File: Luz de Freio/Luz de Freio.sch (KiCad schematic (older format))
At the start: 40 parts, among them J1 Screw_Terminal_01x02, J2 Screw_Terminal_01x02, K1 RELAY_19.1x15.5mm, Q1 BC548, Q2 IRF3205, U1 MC34063AP, U2 TL431DBZ, U3 LM358

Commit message: atualizacao esquematico
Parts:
- added G?: Logo_e-Power_Large, e-Power:Logo_e-Power_16.5x8.0mm_SilkS, symbol e-Power:Logo_e-Power_Large
- added G?: Logo_UFRGS_Large, e-Power:Logo_UFRGS_14.7x8.0mm_SilkS, symbol e-Power:Logo_UFRGS_Large
- added R19: 1R, Resistor_SMD:R_0805_2012Metric, symbol Device:R
- added R20, R21: 10K, Resistor_SMD:R_0805_2012Metric, symbol Device:R
- added R22, R23: 100K, Resistor_SMD:R_0805_2012Metric, symbol Device:R
- added TP1: 24V, e-Power:TestPoint_Pad_D1.0mm, symbol Connector:TestPoint
- added TP2: GND, e-Power:TestPoint_Pad_D1.0mm, symbol Connector:TestPoint
- added TP3: 1.25V, e-Power:TestPoint_Pad_D1.0mm, symbol Connector:TestPoint
- C1: value 100uF -> 220uF; footprint Capacitor_SMD:C_0805_2012Metric_Pad1.15x1.40mm_HandSolder -> e-Power:CP_Elec_10x10
- C3: value 100uF -> 220uF
- D1: value 1N5819 -> SS54HF
- D3, J1, J2: footprint Connector_Phoenix_GMSTB:PhoenixContact_GMSTBA_2,5_2-G-7,62_1x02_P7.62mm_Horizontal -> e-Power:TerminalBlock_Phoenix_MKDS-1,5-2_1x02_P5.08mm_Horizontal_3D
- L1: value 170uH -> 100uH; Loop 50 TURNS -> (none)
- R1: value 0.68R -> 1R; footprint Resistor_SMD:R_0805_2012Metric_Pad1.15x1.40mm_HandSolder -> Resistor_SMD:R_0805_2012Metric
- R2, R5: footprint Resistor_SMD:R_0805_2012Metric_Pad1.15x1.40mm_HandSolder -> Resistor_SMD:R_0805_2012Metric
- R4: value 18K -> ADJ; footprint Resistor_SMD:R_0805_2012Metric_Pad1.15x1.40mm_HandSolder -> Resistor_SMD:R_0805_2012Metric
- U1: footprint Package_DIP:DIP-8_W7.62mm -> Package_SO:SOIC-8_3.9x4.9mm_P1.27mm
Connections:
- net +12V: now also R4.2, R19.2
- net +24V: now also R20.1, R22.2, TP1.1; no longer R4.2
- net GND: now also TP2.1
- net at R5.2, U1.5 (Vfb): now also R21.2, R23.1, TP3.1; no longer R4.1
- net at L1.1, R1.1, R2.2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: now also R4.1, R19.1
- new net: R20.2, R21.1
- new net: R22.1, R23.2
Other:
- moved on the sheet: C1, C2, C3, D1, L1, R1, R2, R5, U1

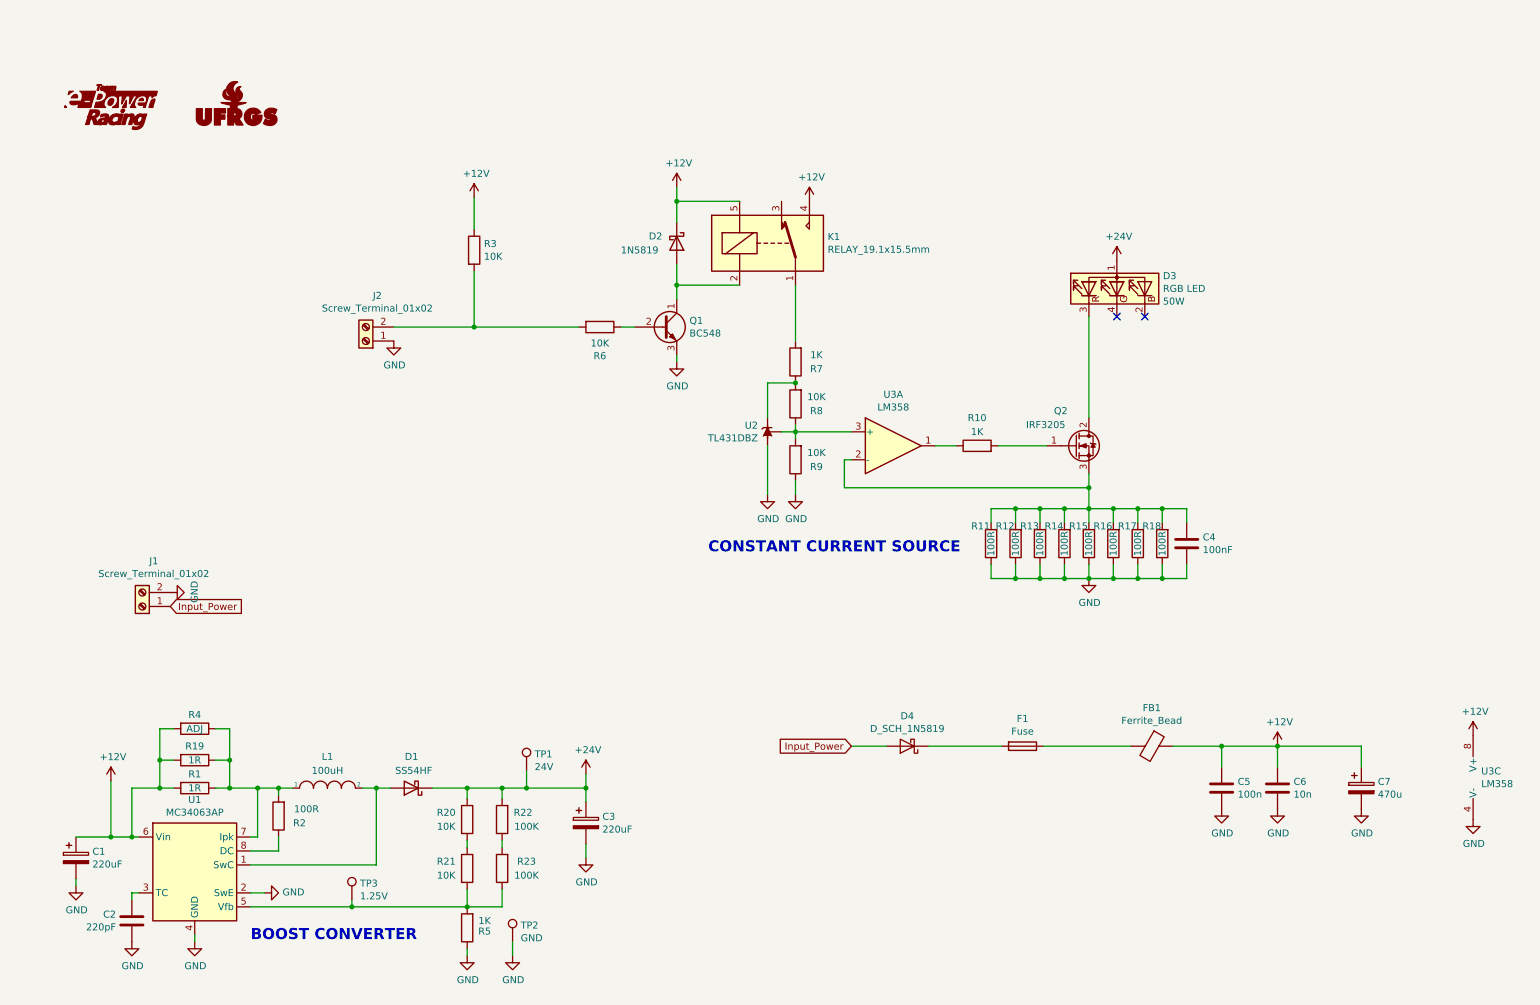
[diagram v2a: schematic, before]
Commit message: Layout Main ECU and Layout Luz de Freio
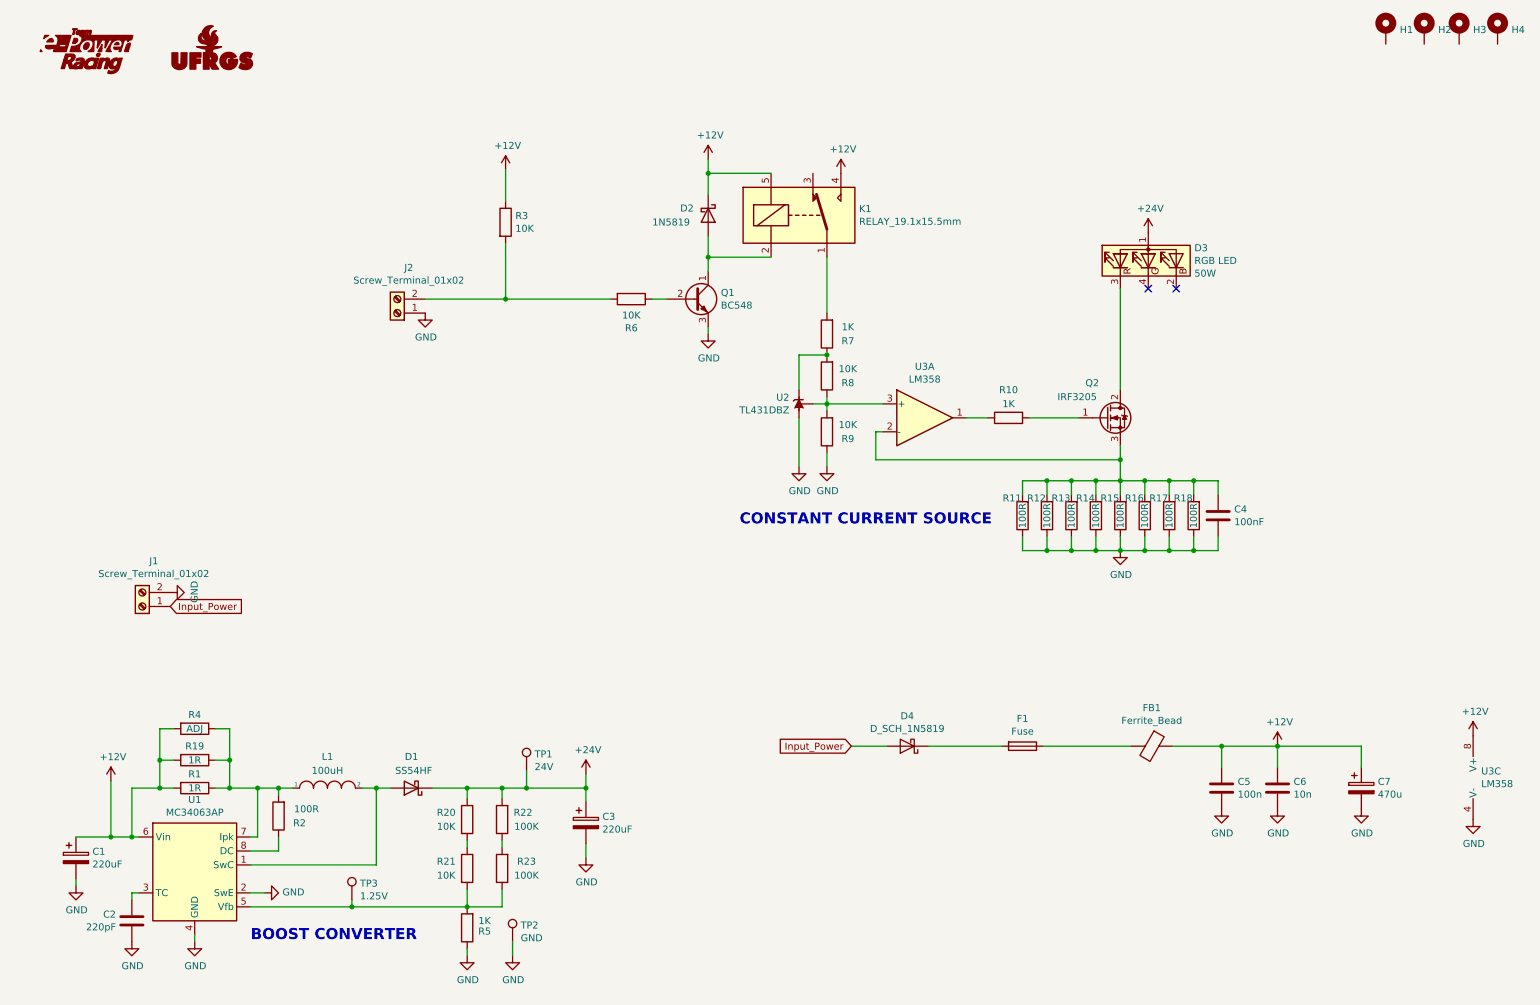
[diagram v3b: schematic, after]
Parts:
- added H1, H2, H3, H4: MountingHole_Pad, e-Power:MountingHole_3.2mm_M3_Pad_Via, symbol Mechanical:MountingHole_Pad
- gave numbers to parts that had none: 2
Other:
- moved on the sheet: C4, D2, D3, J2, K1, Q1, Q2, R10, R11, R12, R13, R14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

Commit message: Fixed Schematic and Layout
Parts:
- removed D2: 1N5819, e-Power:DO-214AC, symbol Diode:1N5819
- removed D4: D_SCH_1N5819, e-Power:DO-214AC, symbol e-Power:D_SCH_1N5819
- removed Q1: BC548, Package_TO_SOT_SMD:SOT-23, symbol Transistor_BJT:BC548
- added C8: 100nF, Capacitor_SMD:C_0805_2012Metric, symbol Device:C
- added C9: 100nF, Capacitor_SMD:C_0805_2012Metric_Pad1.15x1.40mm_HandSolder, symbol Device:C
- added D2, D4: SS54HF, e-Power:DO-214AC, symbol e-Power:SS54HF
- added Q1: Si2302DS, Package_TO_SOT_SMD:SOT-23, symbol e-Power:Si2302DS
- added R24: 10R, Resistor_SMD:R_0805_2012Metric_Pad1.15x1.40mm_HandSolder, symbol Device:R
- added TP4: RED, e-Power:TestPoint_Pad_D1.0mm, symbol Connector:TestPoint
- added TP5: Vref_R, e-Power:TestPoint_Pad_D1.0mm, symbol Connector:TestPoint
- added TP6: RS_R, e-Power:TestPoint_Pad_D1.0mm, symbol Connector:TestPoint
- added TP7: GND, e-Power:TestPoint_Pad_D1.0mm, symbol Connector:TestPoint
- C5: value 100n -> 100nF
- C6: value 10n -> 10nF
- C7: value 470u -> 220uF
- D3, J1, J2: footprint e-Power:TerminalBlock_Phoenix_MKDS-1,5-2_1x02_P5.08mm_Horizontal_3D -> e-Power:TerminalBlock_Phoenix_MKDS-1,5-2_1x02_P5.08mm_Horizontal
- FB1: footprint e-Power:FB_0603_1608Metric -> e-Power:FB_0805_2012Metric
- L1: footprint e-Power:L_10.4x10.4_H4.8 -> e-Power:L_12x12mm_H6mm
- R11, R12, R13, R14, R15, R16, R17, R18: value 100R -> 10R
- R7: value 1K -> 10K
- R8: value 10K -> 1K
- R9: value 10K -> ADJ
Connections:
- net +12V: now also C9.1, D2.1 (K)
- net GND: now also C9.2, Q1.2 (S), R24.1, TP7.1; no longer R11.1, R12.1, R13.1, R14.1, R15.1, R16.1
- net Input_Power: now also D4.2 (A)
- net at K1.2: now also D2.2 (A), Q1.3 (D)
- net at R6.1: now also Q1.1 (G)
- net at D3.3 (RK), Q2.2 (D): now also TP4.1
- net at R8.1, R9.2, U2.2 (REF)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: now also TP5.1
- net at R8.2, U2.1 (K): now also K1.1; no longer R7.1
- net at R10.1, U3.1: now also C8.1
- net at R7.2: now also C4.2, Q2.3 (S), R11.2, R12.2, R13.2, TP6.1; no longer K1.1
- net at F1.2: now also D4.1 (K)
- new net: C8.2, R7.1, U3.2 (-)
- new net: R14.1, R15.1, R16.1, R17.2, R18.2, R24.2
- new net: R11.1, R12.1, R13.1, R14.2, R15.2, R16.2
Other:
- moved on the sheet: C1, C2, C3, C4, C5, C6, C7, D1, D3, F1, FB1, J2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

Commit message: placa fdcan
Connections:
- net GND: now also K1.3
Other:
- note added: "PEDAL PRESSIONADO -> 12V\nPEDAL LIVRE -> 0V"
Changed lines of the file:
@@
 EESchema Schematic File Version 4
-LIBS:Luz de Freio-cache
 EELAYER 30 0
 EELAYER END
@@
 Wire Wire Line
 	7975 4300 7975 4350
+$Comp
+L power:GND #PWR?
+U 1 1 600264D0
+P 5450 1100
+F 0 "#PWR?" H 5450 850 50  0001 C CNN
+F 1 "GND" H 5450 1150 50  0000 C CNN
+F 2 "" H 5450 1100 50  0001 C CNN
+F 3 "" H 5450 1100 50  0001 C CNN
+	1    5450 1100
+	1    0    0    -1
+$EndComp
+Wire Wire Line
+	5450 1100 5600 1100
+Wire Wire Line
+	5600 1100 5600 1150
+Text Notes 2475 2750 0    59   ~ 0
+PEDAL PRESSIONADO -> 12V\nPEDAL LIVRE -> 0V
 $EndSCHEMATC
